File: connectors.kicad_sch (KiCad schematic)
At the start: 23 parts, among them J2 SM08B-SRSS-TB

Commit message: routing
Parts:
- added TP1, TP2, TP3, TP4, TP5, TP6, TP7, TP8: TestPoint, TestPoint:TestPoint_Pad_D1.0mm, symbol Connector:TestPoint
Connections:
- net MOTOR_1: now also TP4.1
- net MOTOR_2: now also TP5.1
- net MOTOR_3: now also TP6.1
- net MOTOR_4: now also TP7.1
- net BEEPER renamed BZ
- new net 5V5_BEC: TP8.1
- new net SWCLK-JTCK: TP1.1
- new net SWDIO-JTMS: TP2.1
- new net VDD_MCU: TP3.1
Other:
- note added: "TEST POINTS FOR DEBUG"

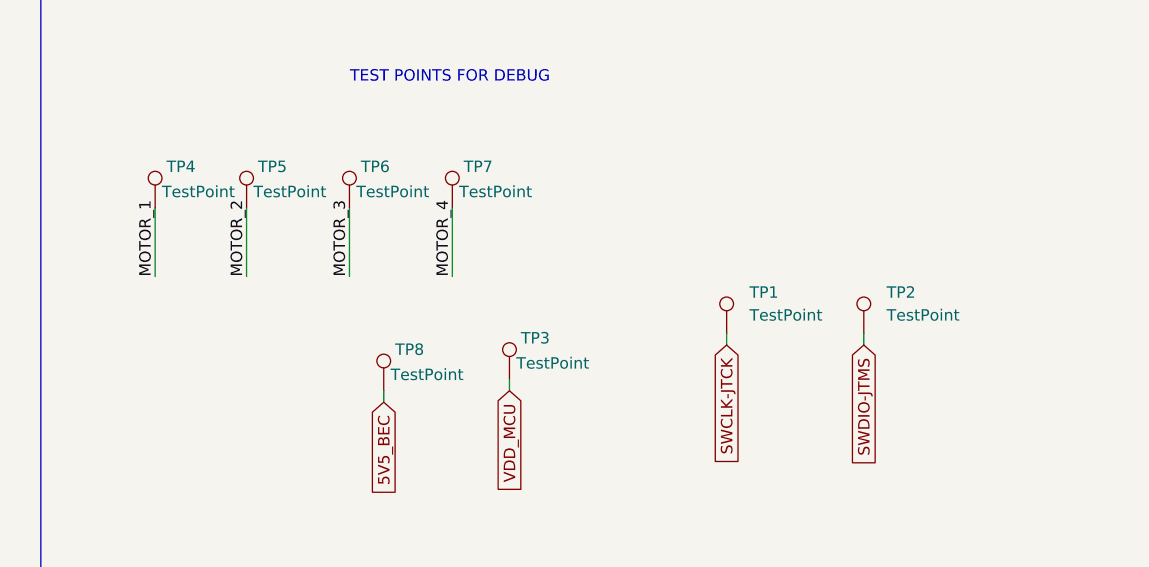
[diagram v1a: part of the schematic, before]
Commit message: update routing and pcb cuts edge
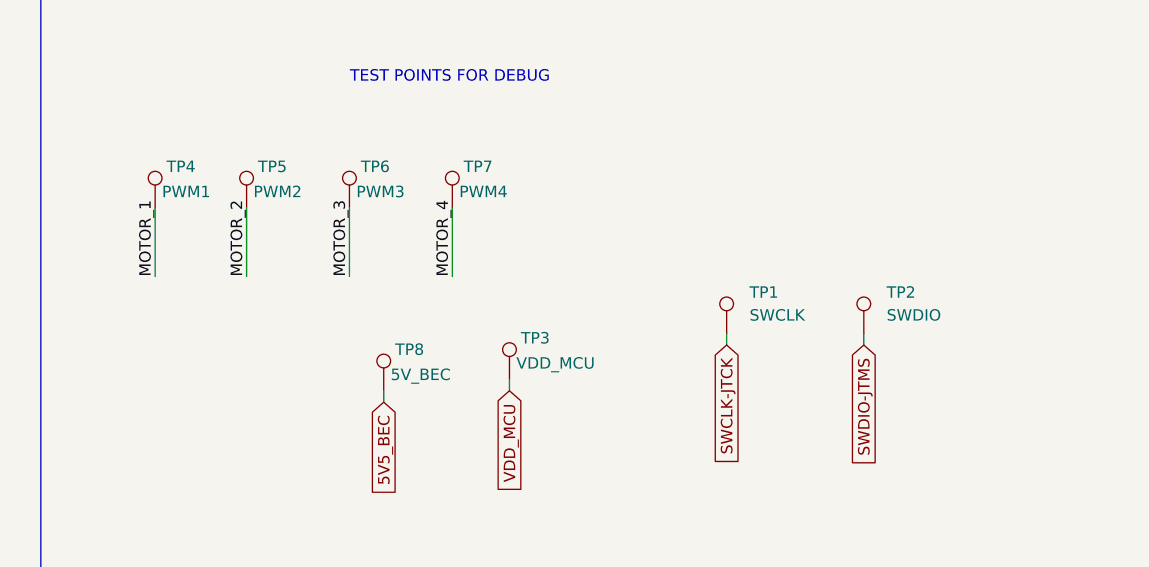
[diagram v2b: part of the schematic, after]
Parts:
- TP1: value TestPoint -> SWCLK
- TP2: value TestPoint -> SWDIO
- TP3: value TestPoint -> VDD_MCU
- TP4: value TestPoint -> PWM1
- TP5: value TestPoint -> PWM2
- TP6: value TestPoint -> PWM3
- TP7: value TestPoint -> PWM4
- TP8: value TestPoint -> 5V_BEC
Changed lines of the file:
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@@
 			)
 		)
-		(property "Value" "TestPoint"
+		(property "Value" "5V_BEC"
 			(at 184.912 150.622 0)
 			(effects
@@
 			)
 		)
-		(property "Value" "TestPoint"
+		(property "Value" "PWM1"
 			(at 159.512 130.302 0)
 			(effects
@@
 			)
 		)
-		(property "Value" "TestPoint"
+		(property "Value" "SWCLK"
 			(at 224.79 144.0179 0)
 			(effects
@@
 			)
 		)
-		(property "Value" "TestPoint"
+		(property "Value" "SWDIO"
 			(at 240.03 144.0179 0)
 			(effects
@@
 			)
 		)
-		(property "Value" "TestPoint"
+		(property "Value" "PWM3"
 			(at 181.102 130.302 0)
 			(effects
@@
 			)
 		)
-		(property "Value" "TestPoint"
+		(property "Value" "VDD_MCU"
 			(at 198.882 149.352 0)
 			(effects
@@
 			)
 		)
-		(property "Value" "TestPoint"
+		(property "Value" "PWM4"
 			(at 192.532 130.302 0)
 			(effects
@@
 			)
 		)
-		(property "Value" "TestPoint"
+		(property "Value" "PWM2"
 			(at 169.672 130.302 0)
 			(effects

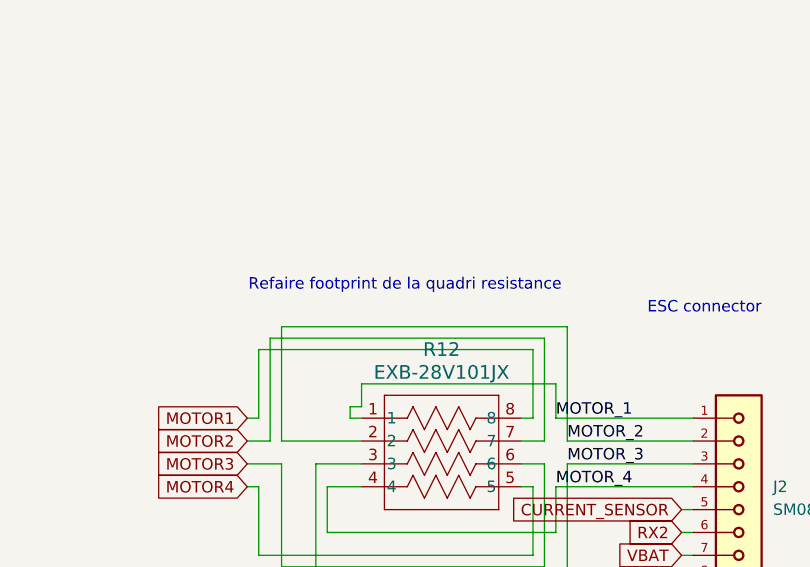
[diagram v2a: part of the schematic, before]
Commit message: Add new Gerber job file for fcg4 project with complete specifications and material stackup
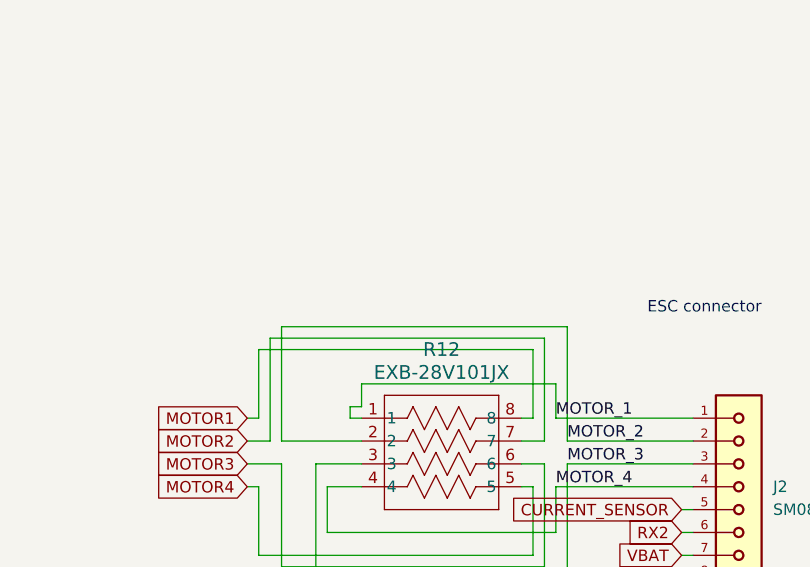
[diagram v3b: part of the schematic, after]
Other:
- note removed: "Refaire footprint de la quadri resistance"
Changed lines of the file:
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@@
 	(generator_version "9.0")
 	(paper "A4")
-	(text "Refaire footprint de la quadri resistance"
-		(exclude_from_sim no)
-		(at 162.306 58.928 0)
-		(effects
-			(font
-				(size 1.27 1.27)
-			)
-		)
-	)
 	(text "TEST POINTS FOR DEBUG\n"
 		(exclude_from_sim no)

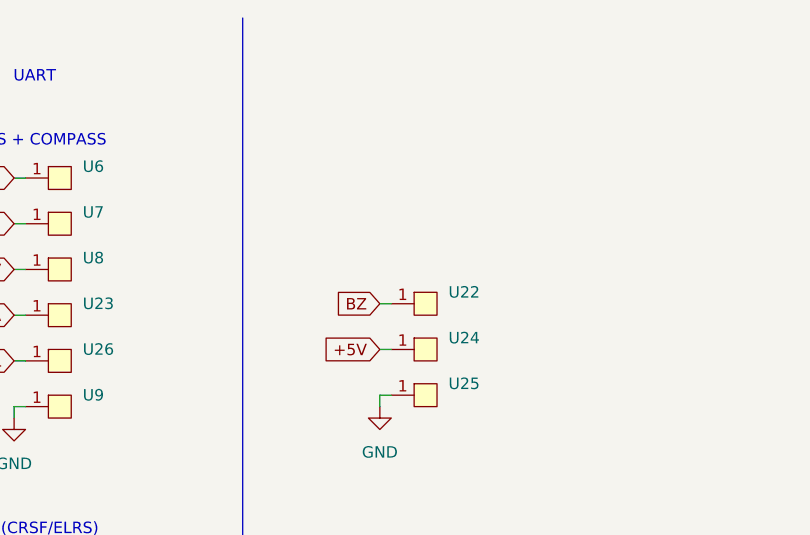
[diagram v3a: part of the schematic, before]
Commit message: Update component properties in schematics with manufacturer details and datasheets
- Added manufacturer name, part number, and LCSC part name for various components in mcu.kicad_sch, power.kicad_sch, and sensor.kicad_sch.
- Updated datasheet links for components to point to the correct URLs.
- Ensured all new properties are hidden in the schematic view.
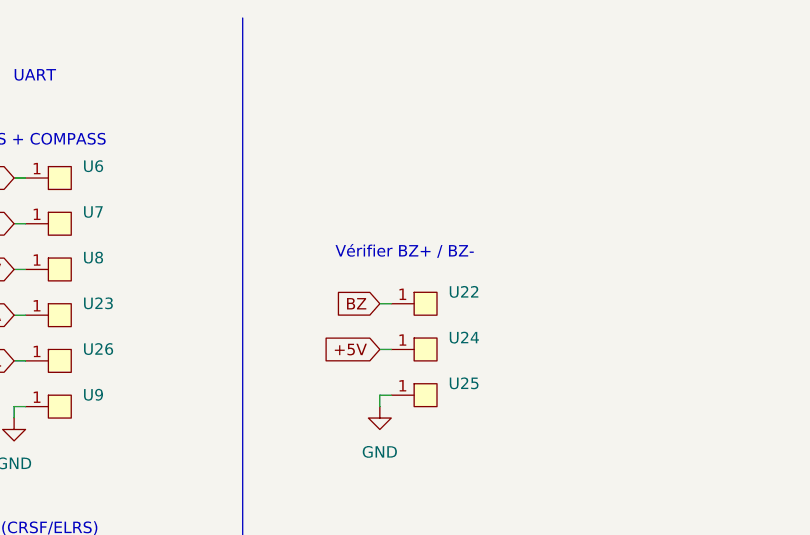
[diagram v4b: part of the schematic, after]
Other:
- note added: "Vérifier BZ+ / BZ-"
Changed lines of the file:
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@@
+		)
+	)
+	(text "Vérifier BZ+ / BZ-"
+		(exclude_from_sim no)
+		(at 76.454 38.862 0)
+		(effects
+			(font
+				(size 1.27 1.27)
+			)
 		)
 	)

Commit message: Almost completed! Update component properties in sensor schematic
- Added datasheets, LCSC part names, manufacturer names, and manufacturer part numbers for various components in the sensor.kicad_sch file.
- Updated the datasheet links for components to point to the correct URLs.
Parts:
- J2: LCSC Part Name (none) -> C160407; Manufacturer_Name (none) -> JST; Manufacturer_Part_Number (none) -> SM08B-SRSS-TB(LF)(SN)
- R12: Manufacturer_Name (none) -> Panasonic; Manufacturer_Part_Number (none) -> EXB-28V101JX; Mouser Part Number (none) -> 667-EXB-28V101JX
- TP1, TP2, TP3, TP4, TP5, TP6, TP7, TP8, U14, U15, U16, U17, U18, U19, U22, U23, U24, U25, U26, U27, U28, U29, U30, U31, U32, U6, U7, U8, U9: now left out of the parts list
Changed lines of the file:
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@@
 		(unit 1)
 		(exclude_from_sim no)
-		(in_bom yes)
+		(in_bom no)
 		(on_board yes)
 		(dnp no)
@@
 		(unit 1)
 		(exclude_from_sim no)
-		(in_bom yes)
+		(in_bom no)
 		(on_board yes)
 		(dnp no)
@@
 		(unit 1)
 		(exclude_from_sim no)
-		(in_bom yes)
+		(in_bom no)
 		(on_board yes)
 		(dnp no)
@@
 		(unit 1)
 		(exclude_from_sim no)
-		(in_bom yes)
+		(in_bom no)
 		(on_board yes)
 		(dnp no)
@@
 		(unit 1)
 		(exclude_from_sim no)
-		(in_bom yes)
+		(in_bom no)
 		(on_board yes)
 		(dnp no)
@@
 		(unit 1)
 		(exclude_from_sim no)
-		(in_bom yes)
+		(in_bom no)
 		(on_board yes)
 		(dnp no)
@@
 		(unit 1)
 		(exclude_from_sim no)
-		(in_bom yes)
+		(in_bom no)
 		(on_board yes)
 		(dnp no)
@@
 		(unit 1)
 		(exclude_from_sim no)
-		(in_bom yes)
+		(in_bom no)
 		(on_board yes)
 		(dnp no)
@@
 		(unit 1)
 		(exclude_from_sim no)
-		(in_bom yes)
+		(in_bom no)
 		(on_board yes)
 		(dnp no)
@@
 		(unit 1)
 		(exclude_from_sim no)
-		(in_bom yes)
+		(in_bom no)
 		(on_board yes)
 		(dnp no)
@@
 		(unit 1)
 		(exclude_from_sim no)
-		(in_bom yes)
+		(in_bom no)
 		(on_board yes)
 		(dnp no)
@@
 		(unit 1)
 		(exclude_from_sim no)
-		(in_bom yes)
+		(in_bom no)
 		(on_board yes)
 		(dnp no)
@@
 			)
 		)
-		(property "Datasheet" ""
+		(property "Datasheet" "https://www.lcsc.com/datasheet/C160407.pdf"
 			(at 199.39 83.82 0)
 			(effects
@@
 			)
 		)
+		(property "LCSC Part Name" "C160407"
+			(at 199.39 83.82 0)
+			(effects
+				(font
+					(size 1.27 1.27)
+				)
+				(hide yes)
+			)
+		)
+		(property "Manufacturer_Name" "JST"
+			(at 199.39 83.82 0)
+			(effects
+				(font
+					(size 1.27 1.27)
+				)
+				(hide yes)
+			)
+		)
+		(property "Manufacturer_Part_Number" "SM08B-SRSS-TB(LF)(SN)"
+			(at 199.39 83.82 0)
+			(effects
+				(font
+					(size 1.27 1.27)
+				)
+				(hide yes)
+			)
+		)
 		(pin "1"
 		)
@@
 		(unit 1)
 		(exclude_from_sim no)
-		(in_bom yes)
+		(in_bom no)
 		(on_board yes)
 		(dnp no)
@@
 		(unit 1)
 		(exclude_from_sim no)
-		(in_bom yes)
+		(in_bom no)
 		(on_board yes)
 		(dnp no)
@@
 		(unit 1)
 		(exclude_from_sim no)
-		(in_bom yes)
+		(in_bom no)
 		(on_board yes)
 		(dnp no)
@@
 		(unit 1)
 		(exclude_from_sim no)
-		(in_bom yes)
+		(in_bom no)
 		(on_board yes)
 		(dnp no)
@@
 		(unit 1)
 		(exclude_from_sim no)
-		(in_bom yes)
+		(in_bom no)
 		(on_board yes)
 		(dnp no)
@@
 		(unit 1)
 		(exclude_from_sim no)
-		(in_bom yes)
+		(in_bom no)
 		(on_board yes)
 		(dnp no)
@@
 		(unit 1)
 		(exclude_from_sim no)
-		(in_bom yes)
+		(in_bom no)
 		(on_board yes)
 		(dnp no)
@@
 		(unit 1)
 		(exclude_from_sim no)
-		(in_bom yes)
+		(in_bom no)
 		(on_board yes)
 		(dnp no)
@@
 		(unit 1)
 		(exclude_from_sim no)
-		(in_bom yes)
+		(in_bom no)
 		(on_board yes)
 		(dnp no)
@@
 		(unit 1)
 		(exclude_from_sim no)
-		(in_bom yes)
+		(in_bom no)
 		(on_board yes)
 		(dnp no)
@@
 		(unit 1)
 		(exclude_from_sim no)
-		(in_bom yes)
+		(in_bom no)
 		(on_board yes)
 		(dnp no)
@@
 		(unit 1)
 		(exclude_from_sim no)
-		(in_bom yes)
+		(in_bom no)
 		(on_board yes)
 		(dnp no)
@@
 		(unit 1)
 		(exclude_from_sim no)
-		(in_bom yes)
+		(in_bom no)
 		(on_board yes)
 		(dnp no)
@@
 			)
 		)
-		(property "Datasheet" "EXB-28V101JX"
+		(property "Datasheet" "https://industrial.panasonic.com/cdbs/www-data/pdf/AOC0000/AOC0000C14.pdf"
 			(at 162.56 60.96 0)
 			(effects
@@
 			)
 		)
+		(property "Manufacturer_Name" "Panasonic"
+			(at 157.48 73.66 0)
+			(effects
+				(font
+					(size 1.27 1.27)
+				)
+				(hide yes)
+			)
+		)
+		(property "Manufacturer_Part_Number" "EXB-28V101JX "
+			(at 157.48 73.66 0)
+			(effects
+				(font
+					(size 1.27 1.27)
+				)
+				(hide yes)
+			)
+		)
+		(property "Mouser Part Number" "667-EXB-28V101JX "
+			(at 157.48 73.66 0)
+			(effects
+				(font
+					(size 1.27 1.27)
+				)
+				(hide yes)
+			)
+		)
 		(pin "7"
 		)
@@
 		(unit 1)
 		(exclude_from_sim no)
-		(in_bom yes)
+		(in_bom no)
 		(on_board yes)
 		(dnp no)
@@
 		(unit 1)
 		(exclude_from_sim no)
-		(in_bom yes)
+		(in_bom no)
 		(on_board yes)
 		(dnp no)
@@
 		(unit 1)
 		(exclude_from_sim no)
-		(in_bom yes)
+		(in_bom no)
 		(on_board yes)
 		(dnp no)
@@
 		(unit 1)
 		(exclude_from_sim no)
-		(in_bom yes)
-		(on_board yes)
-		(dnp no)
+		(in_bom no)
+		(on_board yes)
+		(dnp no)

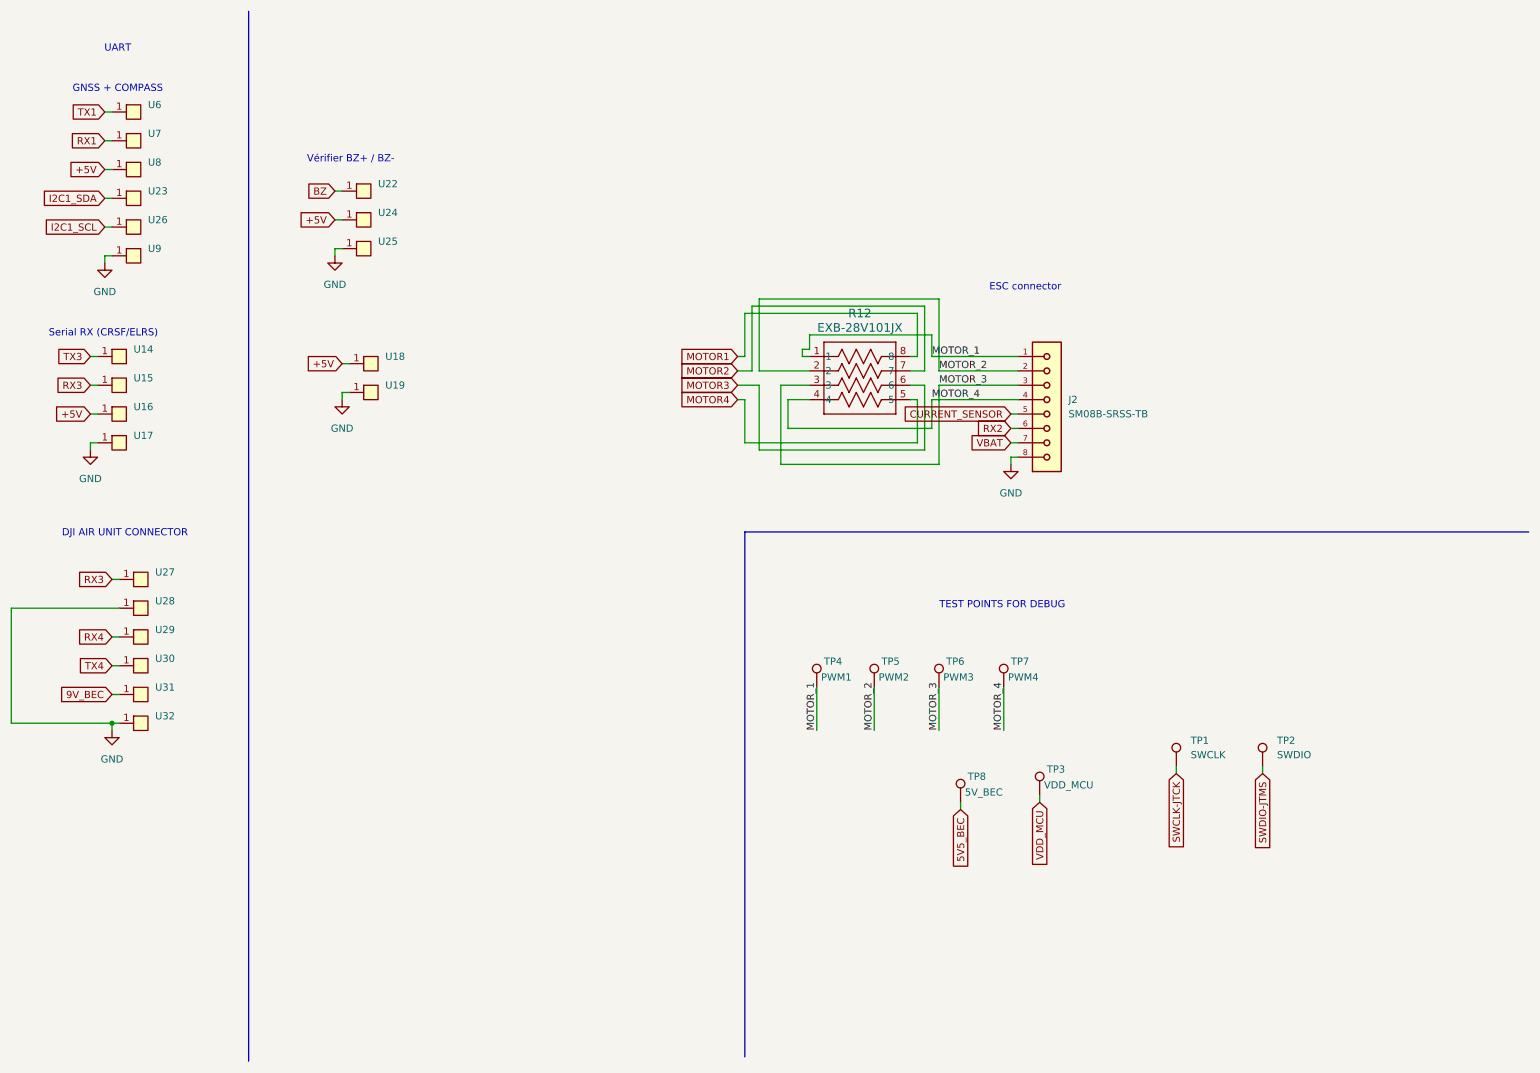
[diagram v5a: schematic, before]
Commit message: PCB v1 ready for manufacturing all the CAM files are available in CAM folder
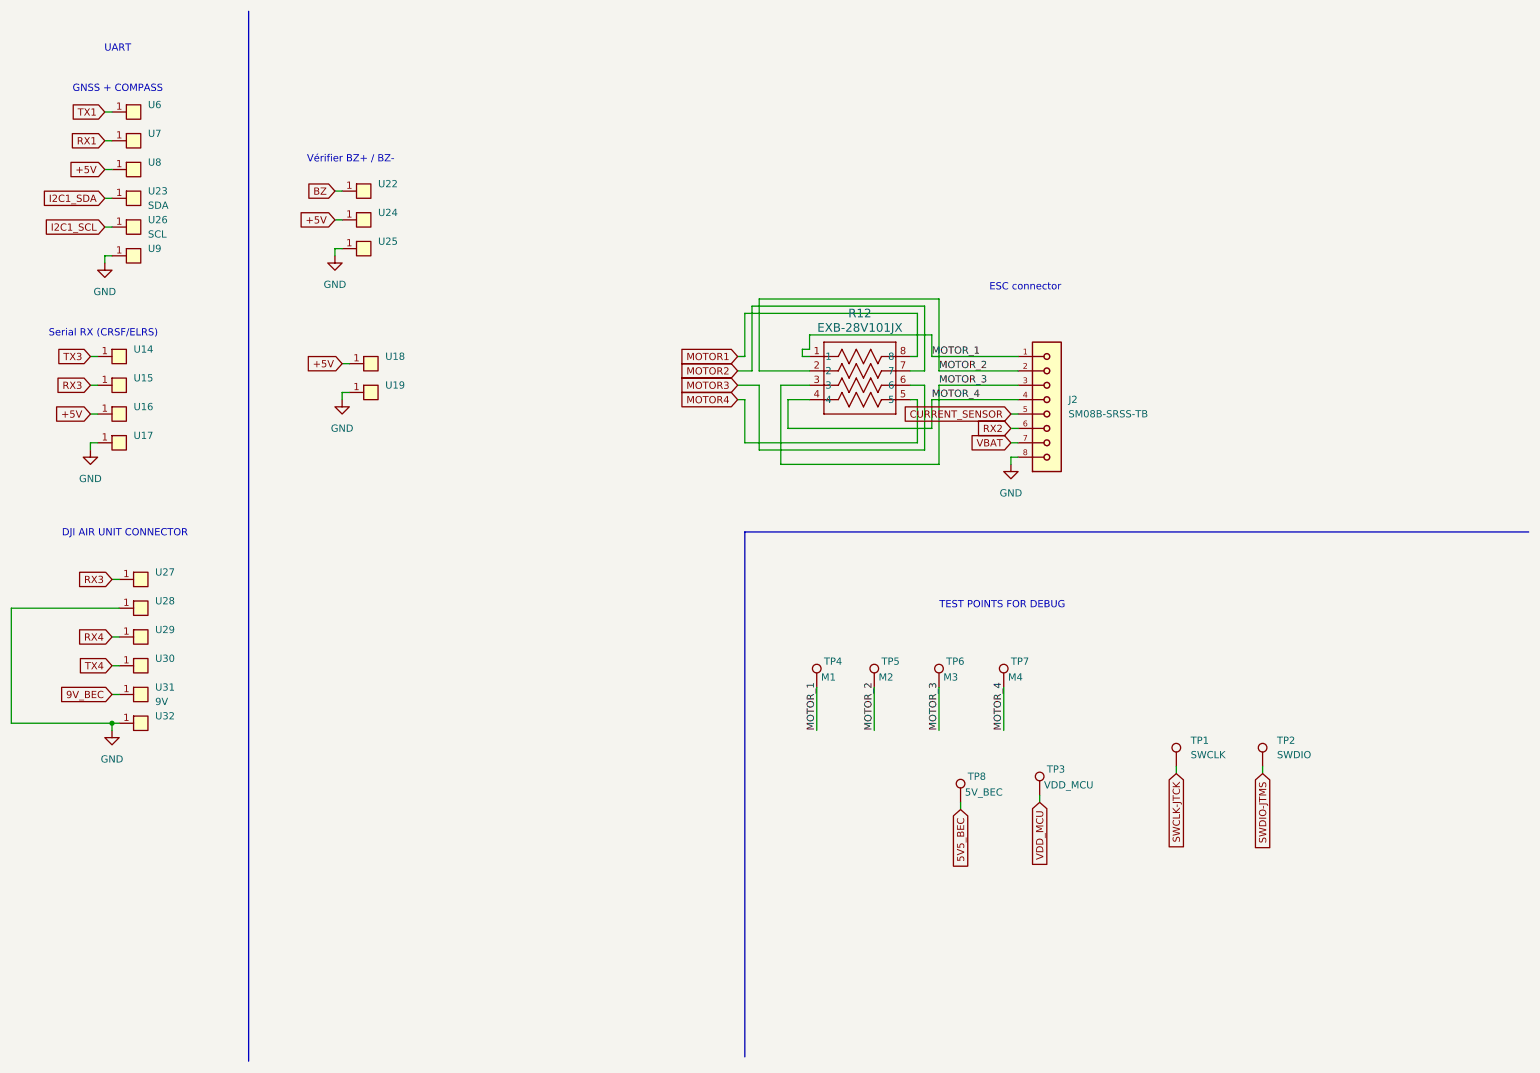
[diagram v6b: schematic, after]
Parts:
- TP4: value PWM1 -> M1
- TP5: value PWM2 -> M2
- TP6: value PWM3 -> M3
- TP7: value PWM4 -> M4
- U23: value ~ -> SDA
- U26: value ~ -> SCL
- U31: value ~ -> 9V
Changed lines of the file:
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@@
 			)
 		)
-		(property "Value" "PWM1"
+		(property "Value" "M1"
 			(at 159.512 130.302 0)
 			(effects
@@
 			)
 		)
-		(property "Value" "~"
+		(property "Value" "SDA"
 			(at 40.64 46.9899 0)
 			(effects
@@
 			)
 		)
-		(property "Value" "~"
+		(property "Value" "SCL"
 			(at 40.64 52.0699 0)
 			(effects
@@
 			)
 		)
-		(property "Value" "PWM3"
+		(property "Value" "M3"
 			(at 181.102 130.302 0)
 			(effects
@@
 			)
 		)
-		(property "Value" "PWM4"
+		(property "Value" "M4"
 			(at 192.532 130.302 0)
 			(effects
@@
 			)
 		)
-		(property "Value" "~"
+		(property "Value" "9V"
 			(at 41.91 134.6199 0)
 			(effects
@@
 			)
 		)
-		(property "Value" "PWM2"
+		(property "Value" "M2"
 			(at 169.672 130.302 0)
 			(effects
